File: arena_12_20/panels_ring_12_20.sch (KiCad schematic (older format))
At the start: 33 parts, among them J1 DB9, P1 COLUMN_0, P10 COLUMN_9, P11 COLUMN_10, P12 COLUMN_11, P13 DIN_5, P14 CONN_5X2, P15 CONN_2, P16 CONN_1, P17 CONN_1, P18 CONN_1, P19 CONN_1, P2 COLUMN_1, P20 CONN_1, P21 CONN_1, P22 CONN_1, P23 CONN_1, P24 CONN_1, P25 CONN_1, P26 CONN_1, P27 CONN_1, P28 CONN_1, P29 CONN_1, P3 COLUMN_2, P4 COLUMN_3, P5 COLUMN_4, P6 COLUMN_5, P7 COLUMN_6, P8 COLUMN_7, P9 COLUMN_8, SW1 SWITCH_INV

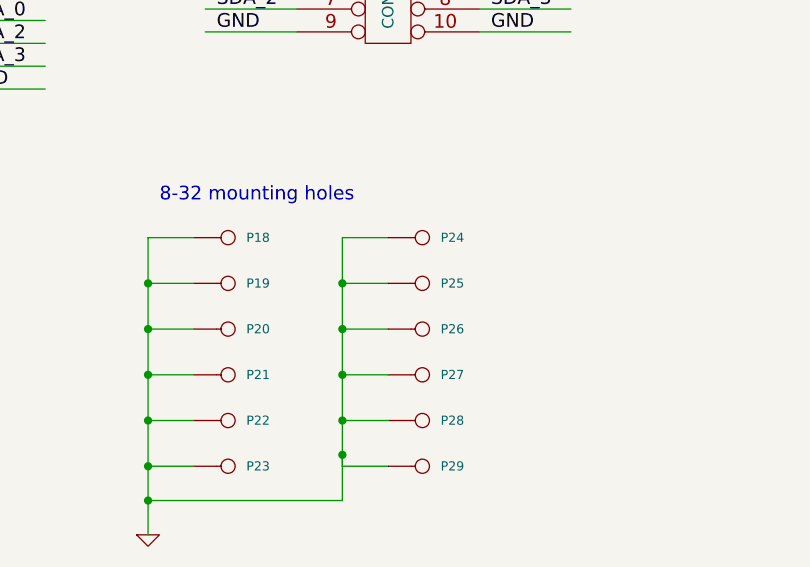
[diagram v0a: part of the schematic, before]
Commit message: Modified board to put DIN5 connector on the left as per Gaby's suggestion.
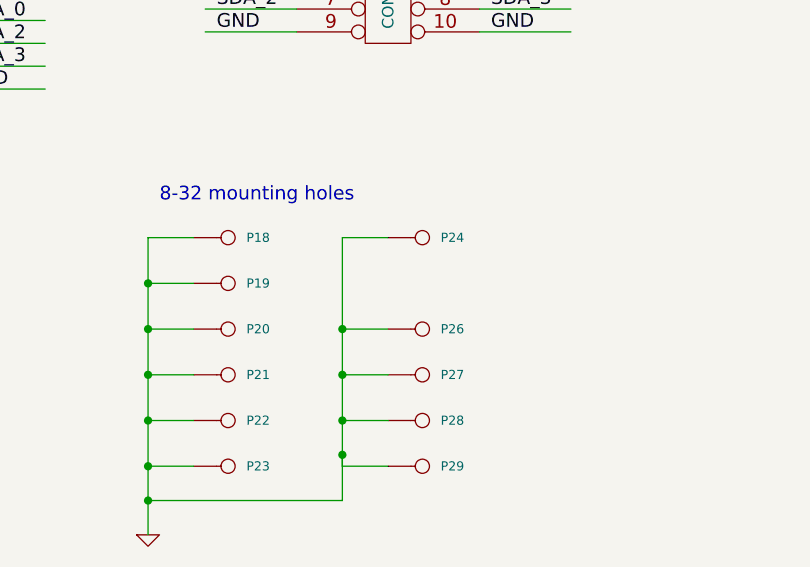
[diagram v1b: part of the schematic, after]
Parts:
- removed P25: CONN_1, symbol CONN_1
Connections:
- wire segments 136 -> 135
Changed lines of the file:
@@
-EESchema Schematic File Version 2  date Mon 27 Dec 2010 05:13:49 PM PST
+EESchema Schematic File Version 2  date Mon 27 Dec 2010 09:34:26 PM PST
 LIBS:power,device,transistors,conn,linear,regul,74xx,cmos4000,adc-dac,memory,xilinx,special,microcontrollers,dsp,microchip,analog_switches,motorola,texas,intel,audio,interface,digital-audio,philips,display,cypress,siliconi,opto,atmel,contrib,valves,./panels_ring_12_20.cache
 EELAYER 24  0
@@
 Wire Wire Line
 	3900 3000 3700 3000
-Connection ~ 3700 2600
-Wire Wire Line
-	3900 2600 3700 2600
 Connection ~ 2850 3400
 Wire Wire Line
@@
 	1    0    0    -1
 $EndComp
-$Comp
-L CONN_1 P25
-U 1 1 4D191121
-P 4050 2600
-F 0 "P25" H 4130 2600 40  0000 L CNN
-F 1 "CONN_1" H 4050 2655 30  0001 C CNN
-	1    4050 2600
-	1    0    0    -1
-$EndComp

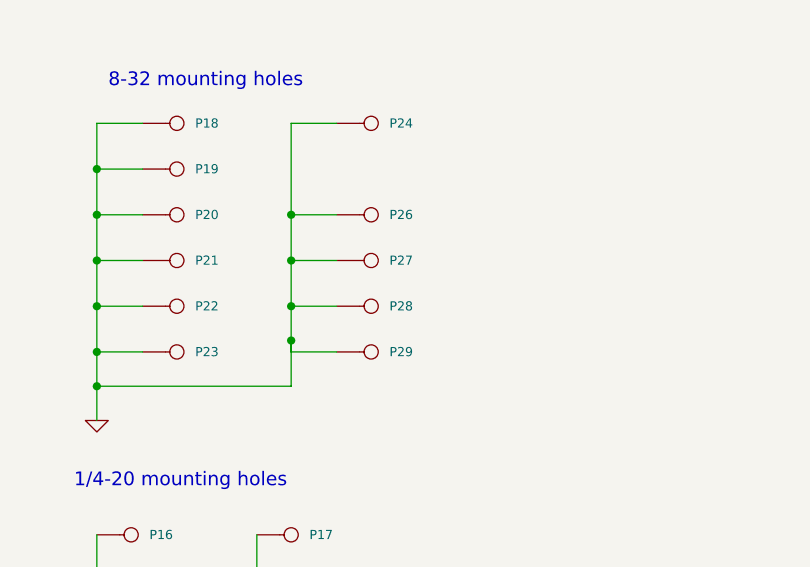
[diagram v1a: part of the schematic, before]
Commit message: Re-routed board so that the db9, din5, switch and jumper are all on the left hand side of the board.
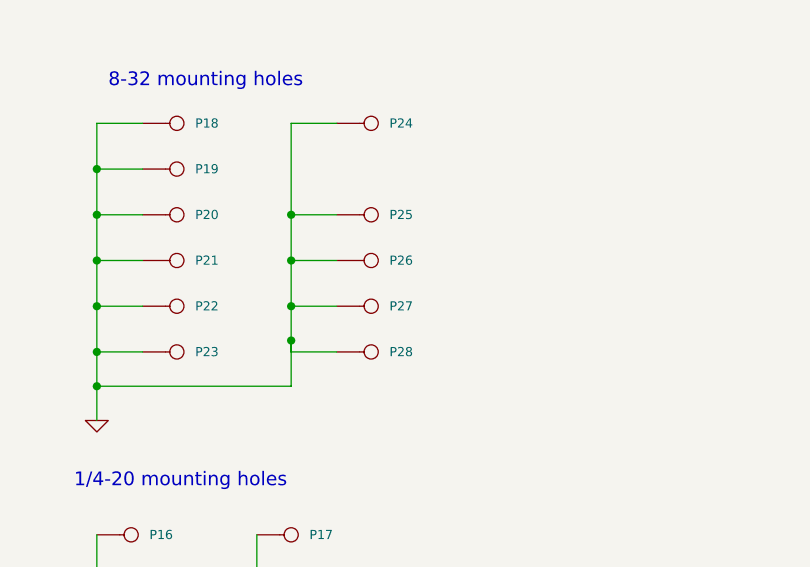
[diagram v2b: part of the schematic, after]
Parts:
- renumbered P26 to P25, P27 to P26, P28 to P27, P29 to P28
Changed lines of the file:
@@
-EESchema Schematic File Version 2  date Mon 27 Dec 2010 09:34:26 PM PST
+EESchema Schematic File Version 2  date Tue 28 Dec 2010 02:13:07 PM PST
 LIBS:power,device,transistors,conn,linear,regul,74xx,cmos4000,adc-dac,memory,xilinx,special,microcontrollers,dsp,microchip,analog_switches,motorola,texas,intel,audio,interface,digital-audio,philips,display,cypress,siliconi,opto,atmel,contrib,valves,./panels_ring_12_20.cache
 EELAYER 24  0
@@
 Connection ~ 3700 3200
 $Comp
-L CONN_1 P29
+L CONN_1 P28
 U 1 1 4D19112A
 P 4050 3400
-F 0 "P29" H 4130 3400 40  0000 L CNN
+F 0 "P28" H 4130 3400 40  0000 L CNN
 F 1 "CONN_1" H 4050 3455 30  0001 C CNN
 	1    4050 3400
@@
 $EndComp
 $Comp
-L CONN_1 P28
+L CONN_1 P27
 U 1 1 4D191129
 P 4050 3200
-F 0 "P28" H 4130 3200 40  0000 L CNN
+F 0 "P27" H 4130 3200 40  0000 L CNN
 F 1 "CONN_1" H 4050 3255 30  0001 C CNN
 	1    4050 3200
@@
 $EndComp
 $Comp
-L CONN_1 P27
+L CONN_1 P26
 U 1 1 4D191126
 P 4050 3000
-F 0 "P27" H 4130 3000 40  0000 L CNN
+F 0 "P26" H 4130 3000 40  0000 L CNN
 F 1 "CONN_1" H 4050 3055 30  0001 C CNN
 	1    4050 3000
@@
 $EndComp
 $Comp
-L CONN_1 P26
+L CONN_1 P25
 U 1 1 4D191125
 P 4050 2800
-F 0 "P26" H 4130 2800 40  0000 L CNN
+F 0 "P25" H 4130 2800 40  0000 L CNN
 F 1 "CONN_1" H 4050 2855 30  0001 C CNN
 	1    4050 2800
